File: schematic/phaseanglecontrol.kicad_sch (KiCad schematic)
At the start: 45 parts, among them J1 L_supply, J2 N_supply, J3 N_motor, J4 L_motor, K1 shutoff, U1 ATtiny26-16P, Y1 16 MHz

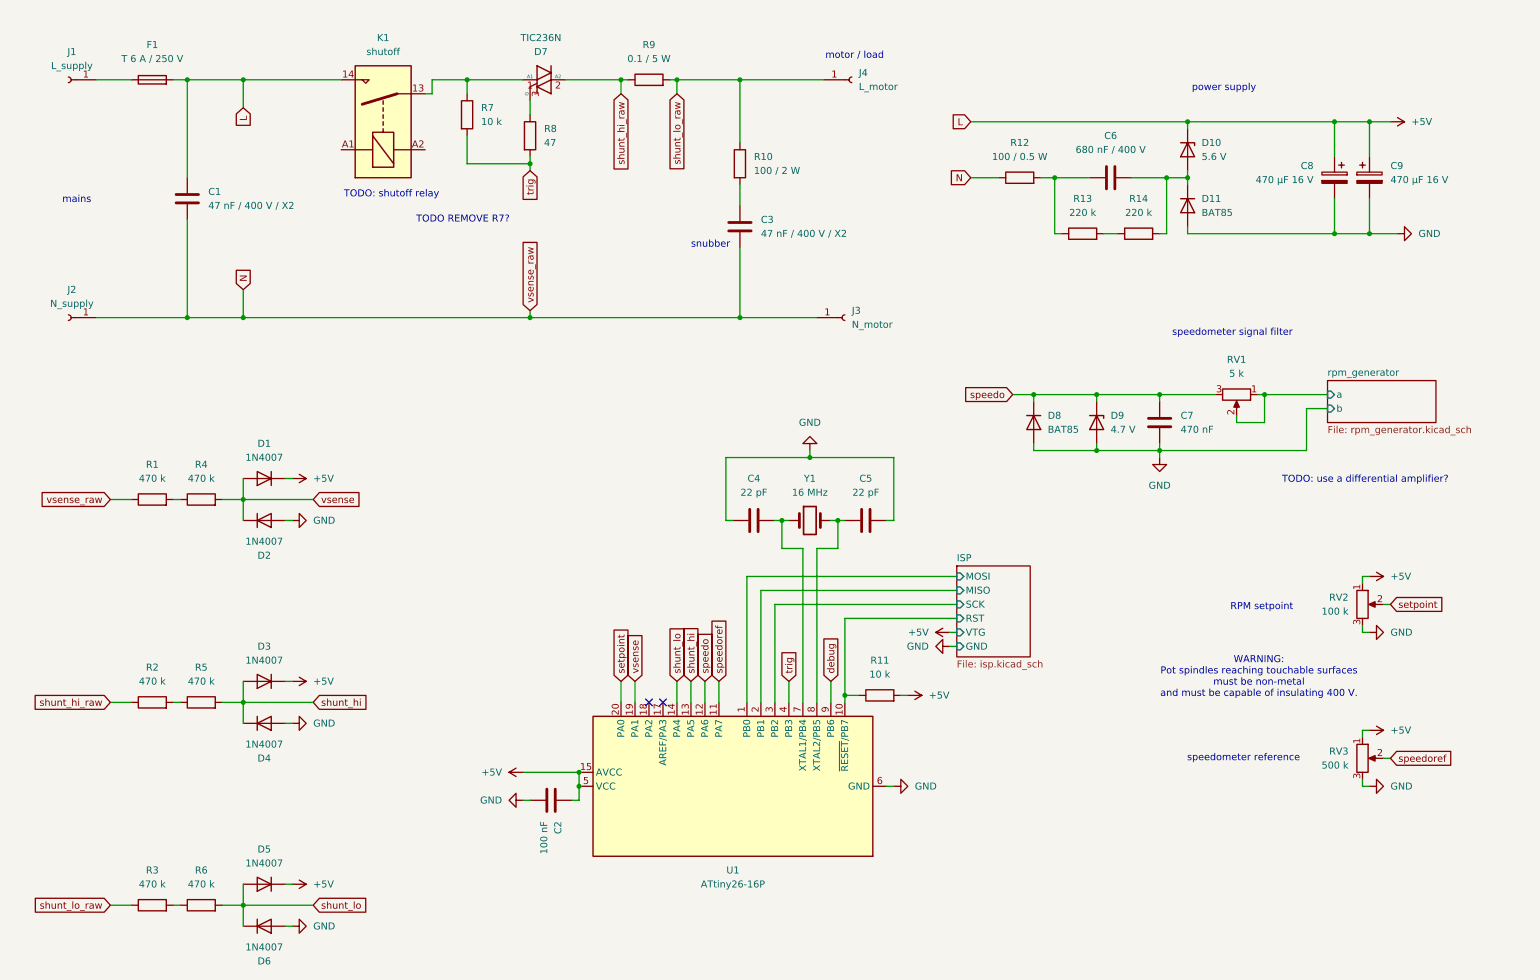
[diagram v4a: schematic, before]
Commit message: schematic: New speedo signal processing
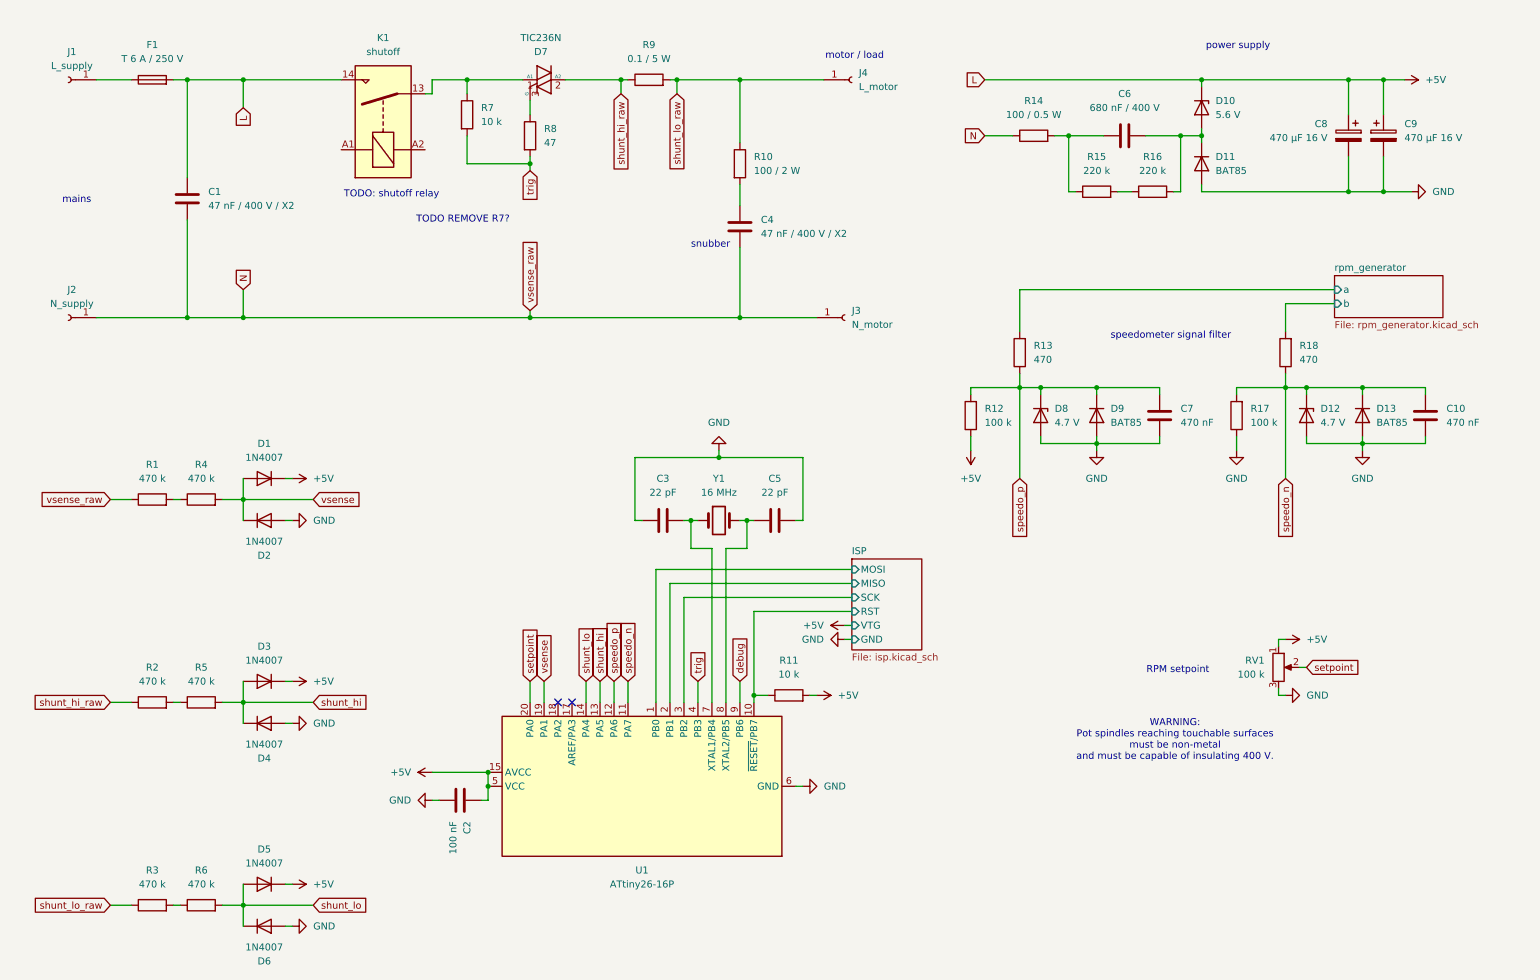
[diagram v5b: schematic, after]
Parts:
- removed D8: BAT85, symbol Device:D
- removed D9: 4.7 V, symbol Device:D_Zener
- removed RV1: 5 k, symbol Device:R_Potentiometer
- removed RV3: 500 k, symbol Device:R_Potentiometer
- added C10: 470 nF, symbol Device:C
- added D12, D8: 4.7 V, symbol Device:D_Zener
- added D13, D9: BAT85, symbol Device:D
- added R12, R17: 100 k, symbol Device:R
- added R13, R18: 470, symbol Device:R
- renumbered C4 to C3, C3 to C4, R12 to R14, R13 to R15, R14 to R16, RV2 to RV1
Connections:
- net +5V: now also R12.1
- net GND: now also C10.2, D12.2 (A), D13.2 (A), D8.2 (A), D9.2 (A), R17.1
- net rpm_generator/a: now also R13.2
- net speedo renamed speedo_p
- net speedo_p: now also D8.1 (K), D9.1 (K), R12.2, R13.1
- net speedoref renamed speedo_n
- net speedo_n: now also C10.1, D12.1 (K), D13.1 (K), R17.2, R18.1
- new net rpm_generator/b: R18.2
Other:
- note removed: "TODO: use a differential amplifier?"
- note removed: "speedometer reference"
- moved on the sheet: C2, C3, C5, C6, C8, C9, D10, D11, R11, R14, R15, R16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

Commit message: Update schematics
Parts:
- removed C10: 470 nF, symbol Device:C
- removed C6: 680 nF / 400 V, symbol Device:C
- removed C8, C9: 470 µF 16 V, symbol Device:C_Polarized
- removed D10: 5.6 V, symbol Device:D_Zener
- removed D11, D13, D9: BAT85, symbol Device:D
- removed D12, D8: 4.7 V, symbol Device:D_Zener
- removed D3, D4, D5, D6: 1N4007, Diode_THT:D_DO-41_SOD81_P10.16mm_Horizontal, symbol Diode:1N4007
- removed K1: shutoff, symbol Relay:Relay_SPST-NO
- removed R12, R17: 100 k, symbol Device:R
- removed R13, R18: 470, symbol Device:R
- removed R14: 100 / 0.5 W, symbol Device:R
- removed R15, R16: 220 k, symbol Device:R
- removed R5, R6: 470 k, symbol Device:R
- removed R9: 0.1 / 5 W, symbol Device:R
- removed RV1: 100 k, symbol Device:R_Potentiometer
- added C2, C3: TODO Y, symbol Device:C
- added D1: P6KE 15CA, Diode_THT:D_DO-201AE_P15.24mm_Horizontal, symbol Diode:1N62xxCA
- added J3: motor_housing, symbol Connector:Conn_01x01_Socket
- added Q1, Q4: IRFP450, Package_TO_SOT_THT:TO-247-3_Vertical, symbol Transistor_FET:IRFP4468PbF
- added Q2: BS170, Package_TO_SOT_THT:TO-92_Inline, symbol Transistor_FET:BS170
- added Q3: IRFR9310, Package_TO_SOT_THT:TO-92_Inline, symbol Transistor_FET:BS250
- added R4: 50 k, symbol Device:R
- C7: value 470 nF -> 1 n
- R2, R3: value 470 k -> 50 k
- renumbered C2 to C1, C3 to C4, C1 to C5, C5 to C6, C4 to C8, D1 to D3, D7 to D4, J3 to J4, J4 to J5, R11 to R1, R4 to R5, R1 to R6, R10 to R9
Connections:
- net +5V: now also C7.1, R2.1, C2.2, D1.2 (A2), Q1.2 (D), Q1.3 (S), Q4.3 (S)
- net GND: now also R3.2, Q2.3 (S); no longer C7.2
- net N: now also C3.1
- net speedo_p: no longer C7.1
- net at D4.1 (A1), R7.1: now also Q4.2 (D)
- net at R2.2: now also C7.2, D1.1 (A1), Q1.1 (G), Q3.1 (D), Q4.1 (G)
- net shunt_hi renamed mot_temp
- net shunt_hi_raw: no longer names the net of D4.2 (A2)
- net shunt_hi_raw: now also J5.1 (Pin_1), R9.1; no longer R2.1
- net shunt_lo renamed n_shutoff
- net n_shutoff: now also R3.1, Q2.2 (G)
- removed net shunt_lo_raw: J5.1 (Pin_1), R3.1, R9.1
- new net: Q2.1 (D), Q3.2 (G), R4.1
- new net: C2.1, C3.2, J3.1 (Pin_1)
- new net +19V: Q3.3 (S), R4.2
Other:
- removed sheet rpm_generator
- added sheet Motor RPM speedometer (speedometer.kicad_sch)
- added sheet Motor temperature NTC (ntc.kicad_sch)
- added sheet Power supply (powersupply.kicad_sch)
- added sheet RPM setpoint (rpm_setpoint.kicad_sch)
- note added: "Primary control"
- note added: "Secondary shut off"
- note added: "TODO: Smaller fuse?"
- note added: "mains supply"
- note added: "mains voltage sensing"
- note removed: "RPM setpoint"
- note removed: "TODO REMOVE R7?"
- note removed: "TODO: shutoff relay"
- note removed: "WARNING: Pot spindles reaching touchable surfaces must be non-metal and must be capable of insulating 400 V."
- note removed: "mains"
- note removed: "power supply"
- note removed: "speedometer signal filter"
- moved on the sheet: C1, C4, C5, C6, C8, D2, D3, D4, J2, J4, J5, R1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

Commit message: Update schematic
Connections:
- net +5V: no longer C7.1, D1.2 (A2), Q1.3 (S), Q4.3 (S), R2.1
- new net: C7.1, D1.2 (A2), Q1.3 (S), Q4.3 (S), R2.1
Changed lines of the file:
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@@
 	)
 	(junction
-		(at 135.89 27.94)
+		(at 137.16 27.94)
 		(diameter 0)
 		(color 0 0 0 0)
@@
 	)
 	(junction
-		(at 137.16 27.94)
-		(diameter 0)
-		(color 0 0 0 0)
-	)
-	(junction
 		(at 173.99 40.64)
 		(diameter 0)
@@
 	)
 	(junction
-		(at 125.73 27.94)
+		(at 92.71 27.94)
 		(diameter 0)
 		(color 0 0 0 0)
@@
 	(junction
 		(at 226.06 27.94)
-		(diameter 0)
-		(color 0 0 0 0)
-	)
-	(junction
-		(at 92.71 27.94)
 		(diameter 0)
 		(color 0 0 0 0)
@@
 	(wire
 		(pts
+			(xy 162.56 55.88) (xy 173.99 55.88)
+		)
+		(stroke
+			(width 0)
+			(type default)
+		)
+	)
+	(wire
+		(pts
+			(xy 222.25 27.94) (xy 226.06 27.94)
+		)
+		(stroke
+			(width 0)
+			(type default)
+		)
+	)
+	(wire
+		(pts
+			(xy 43.18 167.64) (xy 41.91 167.64)
+		)
+		(stroke
+			(width 0)
+			(type default)
+		)
+	)
+	(wire
+		(pts
+			(xy 149.86 62.23) (xy 151.13 62.23)
+		)
+		(stroke
+			(width 0)
+			(type default)
+		)
+	)
+	(wire
+		(pts
+			(xy 193.04 100.33) (xy 189.23 100.33)
+		)
+		(stroke
+			(width 0)
+			(type default)
+		)
+	)
+	(wire
+		(pts
+			(xy 130.81 40.64) (xy 137.16 40.64)
+		)
+		(stroke
+			(width 0)
+			(type default)
+		)
+	)
+	(wire
+		(pts
+			(xy 33.02 167.64) (xy 34.29 167.64)
+		)
+		(stroke
+			(width 0)
+			(type default)
+		)
+	)
+	(wire
+		(pts
+			(xy 173.99 40.64) (xy 173.99 35.56)
+		)
+		(stroke
+			(width 0)
+			(type default)
+		)
+	)
+	(wire
+		(pts
+			(xy 168.91 104.14) (xy 168.91 100.33)
+		)
+		(stroke
+			(width 0)
+			(type default)
+		)
+	)
+	(wire
+		(pts
+			(xy 83.82 121.92) (xy 83.82 149.86)
+		)
+		(stroke
+			(width 0)
+			(type default)
+		)
+	)
+	(wire
+		(pts
+			(xy 60.96 27.94) (xy 60.96 31.75)
+		)
+		(stroke
+			(width 0)
+			(type default)
+		)
+	)
+	(wire
+		(pts
+			(xy 157.48 27.94) (xy 168.91 27.94)
+		)
+		(stroke
+			(width 0)
+			(type default)
+		)
+	)
+	(wire
+		(pts
+			(xy 172.72 100.33) (xy 168.91 100.33)
+		)
+		(stroke
+			(width 0)
+			(type default)
+		)
+	)
+	(wire
+		(pts
+			(xy 90.17 121.92) (xy 86.36 121.92)
+		)
+		(stroke
+			(width 0)
+			(type default)
+		)
+	)
+	(wire
+		(pts
+			(xy 168.91 100.33) (xy 156.21 100.33)
+		)
+		(stroke
+			(width 0)
+			(type default)
+		)
+	)
+	(wire
+		(pts
+			(xy 226.06 58.42) (xy 226.06 68.58)
+		)
+		(stroke
+			(width 0)
+			(type default)
+		)
+	)
+	(wire
+		(pts
+			(xy 68.58 146.05) (xy 68.58 149.86)
+		)
+		(stroke
+			(width 0)
+			(type default)
+		)
+	)
+	(wire
+		(pts
+			(xy 43.18 27.94) (xy 60.96 27.94)
+		)
+		(stroke
+			(width 0)
+			(type default)
+		)
+	)
+	(wire
+		(pts
+			(xy 43.18 162.56) (xy 43.18 165.1)
+		)
+		(stroke
+			(width 0)
+			(type default)
+		)
+	)
+	(wire
+		(pts
+			(xy 205.74 39.37) (xy 205.74 43.18)
+		)
+		(stroke
+			(width 0)
+			(type default)
+		)
+	)
+	(wire
+		(pts
+			(xy 60.96 27.94) (xy 88.9 27.94)
+		)
+		(stroke
+			(width 0)
+			(type default)
+		)
+	)
+	(wire
+		(pts
 			(xy 92.71 27.94) (xy 125.73 27.94)
 		)
@@
 	(wire
 		(pts
-			(xy 162.56 55.88) (xy 173.99 55.88)
-		)
-		(stroke
-			(width 0)
-			(type default)
-		)
-	)
-	(wire
-		(pts
-			(xy 222.25 27.94) (xy 226.06 27.94)
-		)
-		(stroke
-			(width 0)
-			(type default)
-		)
-	)
-	(wire
-		(pts
-			(xy 137.16 27.94) (xy 135.89 27.94)
-		)
-		(stroke
-			(width 0)
-			(type default)
-		)
-	)
-	(wire
-		(pts
-			(xy 43.18 167.64) (xy 41.91 167.64)
-		)
-		(stroke
-			(width 0)
-			(type default)
-		)
-	)
-	(wire
-		(pts
-			(xy 149.86 62.23) (xy 151.13 62.23)
-		)
-		(stroke
-			(width 0)
-			(type default)
-		)
-	)
-	(wire
-		(pts
-			(xy 193.04 100.33) (xy 189.23 100.33)
-		)
-		(stroke
-			(width 0)
-			(type default)
-		)
-	)
-	(wire
-		(pts
-			(xy 130.81 40.64) (xy 137.16 40.64)
-		)
-		(stroke
-			(width 0)
-			(type default)
-		)
-	)
-	(wire
-		(pts
-			(xy 33.02 167.64) (xy 34.29 167.64)
-		)
-		(stroke
-			(width 0)
-			(type default)
-		)
-	)
-	(wire
-		(pts
-			(xy 173.99 40.64) (xy 173.99 35.56)
-		)
-		(stroke
-			(width 0)
-			(type default)
-		)
-	)
-	(wire
-		(pts
-			(xy 168.91 104.14) (xy 168.91 100.33)
-		)
-		(stroke
-			(width 0)
-			(type default)
-		)
-	)
-	(wire
-		(pts
-			(xy 83.82 121.92) (xy 83.82 149.86)
-		)
-		(stroke
-			(width 0)
-			(type default)
-		)
-	)
-	(wire
-		(pts
-			(xy 60.96 27.94) (xy 60.96 31.75)
-		)
-		(stroke
-			(width 0)
-			(type default)
-		)
-	)
-	(wire
-		(pts
-			(xy 157.48 27.94) (xy 168.91 27.94)
-		)
-		(stroke
-			(width 0)
-			(type default)
-		)
-	)
-	(wire
-		(pts
-			(xy 172.72 100.33) (xy 168.91 100.33)
-		)
-		(stroke
-			(width 0)
-			(type default)
-		)
-	)
-	(wire
-		(pts
-			(xy 90.17 121.92) (xy 86.36 121.92)
-		)
-		(stroke
-			(width 0)
-			(type default)
-		)
-	)
-	(wire
-		(pts
-			(xy 168.91 100.33) (xy 156.21 100.33)
-		)
-		(stroke
-			(width 0)
-			(type default)
-		)
-	)
-	(wire
-		(pts
-			(xy 226.06 58.42) (xy 226.06 68.58)
-		)
-		(stroke
-			(width 0)
-			(type default)
-		)
-	)
-	(wire
-		(pts
-			(xy 68.58 146.05) (xy 68.58 149.86)
-		)
-		(stroke
-			(width 0)
-			(type default)
-		)
-	)
-	(wire
-		(pts
-			(xy 43.18 27.94) (xy 60.96 27.94)
-		)
-		(stroke
-			(width 0)
-			(type default)
-		)
-	)
-	(wire
-		(pts
-			(xy 43.18 162.56) (xy 43.18 165.1)
-		)
-		(stroke
-			(width 0)
-			(type default)
-		)
-	)
-	(wire
-		(pts
-			(xy 205.74 39.37) (xy 205.74 43.18)
-		)
-		(stroke
-			(width 0)
-			(type default)
-		)
-	)
-	(wire
-		(pts
-			(xy 135.89 27.94) (xy 125.73 27.94)
-		)
-		(stroke
-			(width 0)
-			(type default)
-		)
-	)
-	(wire
-		(pts
-			(xy 60.96 27.94) (xy 88.9 27.94)
-		)
-		(stroke
-			(width 0)
-			(type default)
-		)
-	)
-	(wire
-		(pts
 			(xy 80.01 116.84) (xy 80.01 121.92)
 		)
@@
 		)
 		(stroke
+			(width 0)
+			(type default)
+		)
+	)
+	(wire
+		(pts
+			(xy 135.89 27.94) (xy 137.16 27.94)
+		)
+		(stroke

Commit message: Update schematic
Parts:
- C2, C3: value TODO Y -> 2.2 nF / 300 V / Y2
- C5: value 47 nF / 400 V / X2 -> 220 nF / 300 V / X2
- F1: value T 6 A / 250 V -> T 2 A / 250 V
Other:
- note removed: "TODO: Smaller fuse?"
- moved on the sheet: C8, R9
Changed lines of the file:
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@@
 	(text "snubber"
 		(exclude_from_sim no)
-		(at 231.394 49.022 0)
+		(at 245.364 49.022 0)
 		(effects
 			(font
@@
 		)
 	)
-	(text "TODO: Smaller fuse?"
-		(exclude_from_sim no)
-		(at 48.514 17.018 0)
-		(effects
-			(font
-				(size 1.27 1.27)
-			)
-		)
-	)
 	(text "Primary control"
 		(exclude_from_sim no)
@@
 	)
 	(junction
+		(at 240.03 68.58)
+		(diameter 0)
+		(color 0 0 0 0)
+	)
+	(junction
 		(at 139.7 53.34)
 		(diameter 0)
@@
 	)
 	(junction
+		(at 240.03 27.94)
+		(diameter 0)
+		(color 0 0 0 0)
+	)
+	(junction
 		(at 173.99 40.64)
 		(diameter 0)
@@
 	)
 	(junction
-		(at 226.06 68.58)
-		(diameter 0)
-		(color 0 0 0 0)
-	)
-	(junction
-		(at 226.06 27.94)
-		(diameter 0)
-		(color 0 0 0 0)
-	)
-	(junction
 		(at 173.99 55.88)
 		(diameter 0)
@@
 	(wire
 		(pts
-			(xy 193.04 68.58) (xy 226.06 68.58)
+			(xy 193.04 68.58) (xy 240.03 68.58)
 		)
 		(stroke
@@
 	(wire
 		(pts
-			(xy 138.43 53.34) (xy 139.7 53.34)
+			(xy 132.08 53.34) (xy 139.7 53.34)
 		)
 		(stroke
@@
 	(wire
 		(pts
-			(xy 226.06 27.94) (xy 226.06 39.37)
+			(xy 240.03 27.94) (xy 240.03 39.37)
 		)
 		(stroke
@@
 	(wire
 		(pts
+			(xy 240.03 68.58) (xy 262.89 68.58)
+		)
+		(stroke
+			(width 0)
+			(type default)
+		)
+	)
+	(wire
+		(pts
 			(xy 173.99 40.64) (xy 173.99 41.91)
 		)
@@
 	(wire
 		(pts
-			(xy 226.06 68.58) (xy 262.89 68.58)
-		)
-		(stroke
-			(width 0)
-			(type default)
-		)
-	)
-	(wire
-		(pts
 			(xy 60.96 39.37) (xy 60.96 48.26)
 		)
@@
 	(wire
 		(pts
-			(xy 215.9 43.18) (xy 215.9 44.45)
+			(xy 215.9 43.18) (xy 215.9 49.53)
 		)
 		(stroke
@@
 	(wire
 		(pts
-			(xy 222.25 27.94) (xy 226.06 27.94)
+			(xy 222.25 27.94) (xy 240.03 27.94)
 		)
 		(stroke
@@
 	(wire
 		(pts
-			(xy 226.06 58.42) (xy 226.06 68.58)
+			(xy 240.03 58.42) (xy 240.03 68.58)
 		)
 		(stroke
@@
 	(wire
 		(pts
+			(xy 240.03 27.94) (xy 264.16 27.94)
+		)
+		(stroke
+			(width 0)
+			(type default)
+		)
+	)
+	(wire
+		(pts
 			(xy 137.16 27.94) (xy 137.16 30.48)
 		)
@@
 	(wire
 		(pts
-			(xy 226.06 46.99) (xy 226.06 50.8)
+			(xy 240.03 46.99) (xy 240.03 50.8)
 		)
 		(stroke
@@
 	(wire
 		(pts
-			(xy 226.06 27.94) (xy 264.16 27.94)
-		)
-		(stroke
-			(width 0)
-			(type default)
-		)
-	)
-	(wire
-		(pts
 			(xy 69.85 105.41) (xy 85.09 105.41)
 		)
@@
 	(global_label "trig"
 		(shape input)
-		(at 215.9 44.45 270)
+		(at 215.9 49.53 270)
 		(fields_autoplaced yes)
 		(effects
@@
 		)
 		(property "Intersheetrefs" "${INTERSHEET_REFS}"
-			(at 215.9 50.7009 90)
+			(at 215.9 55.7809 90)
 			(effects
 				(font
@@
 	(global_label "n_shutoff"
 		(shape input)
-		(at 138.43 53.34 180)
+		(at 132.08 53.34 180)
 		(fields_autoplaced yes)
 		(effects
@@
 		)
 		(property "Intersheetrefs" "${INTERSHEET_REFS}"
-			(at 126.676 53.34 0)
+			(at 120.326 53.34 0)
 			(effects
 				(font
@@
 	(symbol
 		(lib_id "Device:R")
-		(at 226.06 43.18 0)
+		(at 240.03 43.18 0)
 		(unit 1)
 		(exclude_from_sim no)
@@
 		(fields_autoplaced yes)
 		(property "Reference" "R9"
-			(at 228.6 41.9099 0)
+			(at 242.57 41.9099 0)
 			(effects
 				(font
@@
 		)
 		(property "Value" "100 / 2 W"
-			(at 228.6 44.4499 0)
+			(at 242.57 44.4499 0)
 			(effects
 				(font
@@
 		)
 		(property "Footprint" ""
-			(at 224.282 43.18 90)
+			(at 238.252 43.18 90)
 			(effects
 				(font
@@
 		)
 		(property "Datasheet" "~"
-			(at 226.06 43.18 0)
+			(at 240.03 43.18 0)
 			(effects
 				(font
@@
 		)
 		(property "Description" "Resistor"
-			(at 226.06 43.18 0)
+			(at 240.03 43.18 0)
 			(effects
 				(font
@@
 			)
 		)
-		(property "Value" "T 6 A / 250 V"
+		(property "Value" "T 2 A / 250 V"
 			(at 39.37 24.13 90)
 			(effects
@@
 			)
 		)
-		(property "Value" "TODO Y"
+		(property "Value" "2.2 nF / 300 V / Y2"
 			(at 57.15 36.8299 0)
 			(effects
@@
 			)
 		)
-		(property "Value" "TODO Y"
+		(property "Value" "2.2 nF / 300 V / Y2"
 			(at 57.15 62.2299 0)
 			(effects
@@
 	(symbol
 		(lib_id "Device:C")
-		(at 226.06 54.61 0)
+		(at 240.03 54.61 0)
 		(unit 1)
 		(exclude_from_sim no)
@@
 		(fields_autoplaced yes)
 		(property "Reference" "C8"
-			(at 229.87 53.3399 0)
+			(at 243.84 53.3399 0)
 			(effects
 				(font
@@
 		)
 		(property "Value" "47 nF / 400 V / X2"
-			(at 229.87 55.8799 0)
+			(at 243.84 55.8799 0)
 			(effects
 				(font
@@
 		)
 		(property "Footprint" ""
-			(at 227.0252 58.42 0)
+			(at 240.9952 58.42 0)
 			(effects
 				(font
@@
 		)
 		(property "Datasheet" "~"
-			(at 226.06 54.61 0)
+			(at 240.03 54.61 0)
 			(effects
 				(font
@@
 		)
 		(property "Description" "Unpolarized capacitor"
-			(at 226.06 54.61 0)
+			(at 240.03 54.61 0)
 			(effects
 				(font
@@
 			)
 		)
-		(property "Value" "47 nF / 400 V / X2"
+		(property "Value" "220 nF / 300 V / X2"
 			(at 85.09 49.5299 0)
 			(effects
